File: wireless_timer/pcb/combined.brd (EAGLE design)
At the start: 36 x 76.5 mm, 51 parts, among them U1 ATTINY1616-SNR

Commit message: ready for dcdc insertion
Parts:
- removed C8: 10uF, rcl:C0805
- moved D1 12.4 mm to (8.52, 33.8), turned to 180 degrees
- moved R21 9.14 mm to (32.7, 25.8)
- moved C9 5.55 mm to (14.1, 35.6)
- moved JP3 4.20 mm to (33.9, 36.3)
- moved TP4 4.20 mm to (19.2, 51.3)
- moved JP5 4.20 mm to (33.8, 45.8)
- moved R1 4.20 mm to (22.0, 47.5)
- moved R16 4.20 mm to (30.4, 46.9)
- moved R18 4.20 mm to (31.2, 35.6)
- moved R2 4.20 mm to (19.7, 47.5)
- moved TP5 4.20 mm to (25.2, 51.3)
- moved C1 4.20 mm to (17.8, 47.6)
- moved R15 4.20 mm to (30.4, 49.1)
- moved R17 4.20 mm to (31.3, 43.5)
- moved R20 4.20 mm to (24.2, 47.6)
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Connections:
- net GND: no longer C8.2
- net VCC: no longer C8.1

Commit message: layout completed
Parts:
- added C17, C18, C19: 10uF, rcl:C0805
- added D2, D3: BAT, diode:SOD-123_MINI-SMA
- added JP6, JP7: (no value), pinhead-2:1X02-S
- added L1: 1uH, 5040_INDUCTOR:IND_74404043220A
- added R22, R23: 100K, rcl:R0805
- added R38: 511K, rcl:M0805
- added R39: 91K, rcl:M0805
- added R45: 50K, rcl:M0805
- added U2: TPS, TPS63000DRLR:SOTFL50P160X60-8N
- added U3, U4: PMOS, DMP3165L:SOT103P240X110-3N
- S1, S2, S3, S4, S5, S6: value SW_55MM -> SW
- TP1, TP5: value TPTP18R -> GND
- TP2: value TPTP18R -> VDD
- TP3: value TPTP18R -> VCC
- TP4: value TPTP18R -> VBAT
- U1: value ATTINY1616-SNR -> 1
- moved D1 27.7 mm to (7.12, 61.5), flipped to the bottom, turned to 270 degrees
- moved TP4 19.1 mm to (32.4, 65.2), turned to 180 degrees
- moved TP3 14.7 mm to (23.1, 57.6)
- moved TP2 14.2 mm to (15.3, 51.3), turned to 270 degrees
- moved R21 13.6 mm to (31.3, 39.4), flipped to the bottom
- moved TP5 6.75 mm to (18.5, 51.3)
- moved JP4 6.17 mm to (32.5, 61.1), flipped to the top
- moved JP2 5.23 mm to (3.60, 61.1), flipped to the bottom
- moved C9 0.88 mm to (14.0, 36.5), turned to 270 degrees
- moved R3 0.53 mm to (24.1, 31.7)
- moved R18 0.44 mm to (31.2, 35.2)
- moved R4 0.42 mm to (24.1, 29.4)
- moved C1 0.32 mm to (17.4, 47.5)
- moved C2 0.30 mm to (24.1, 27.1)
- moved R1 0.07 mm to (21.9, 47.6)
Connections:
- new net DC_SW: R22.1, U1.3, U3.1
- new net LX1: L1.2, U2.3
- new net LX2: L1.1, U2.2
- new net N$27: R38.1, R39.2, U2.8
- new net N$36: R45.2, U2.5
- new net VBAT_O: D1.A, D3.A, JP6.2, JP7.2, R1.2, R22.2, U3.2
- new net VCC_SW: R23.2, U1.5, U4.1
- new net VIN: C17.1, D3.C, U2.4, U3.3
- net GND: now also C17.2, C18.2, C19.2, R39.1, R45.1, U2.7
- net S6: no longer TP3.TP
- net SHDN: now also U2.6
- net VBAT: now also JP6.1, JP7.1; no longer D1.A, R1.2
- net VCC: now also C18.1, C19.1, D2.A, R23.1, R38.2, TP3.TP, U2.1, U4.2
- net VDD: now also D2.C, U4.3
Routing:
- net GND: track 0.00 -> 307.2 mm, vias 0 -> 5
- net VCC: track 0.00 -> 191.0 mm, vias 0 -> 9
- net VDD: track 0.00 -> 100.5 mm, vias 0 -> 1
- net SCL: track 0.00 -> 88.3 mm, vias 0 -> 2
- net S3: track 0.00 -> 60.7 mm, vias 0 -> 3
- net VBAT_O: track 0.00 -> 45.7 mm, vias 0 -> 1
- net VBAT: track 0.00 -> 43.7 mm
- net S6: track 0.00 -> 37.4 mm, vias 0 -> 3
- net S4: track 0.00 -> 34.6 mm, vias 0 -> 3
- net S2: track 0.00 -> 29.7 mm, vias 0 -> 3
- net SDA: track 0.00 -> 28.0 mm, vias 0 -> 3
- net DC_SW: track 0.00 -> 27.8 mm, vias 0 -> 2
- net SHDN: track 0.00 -> 25.4 mm, vias 0 -> 3
- net SET: track 0.00 -> 24.4 mm, vias 0 -> 4
- net S5: track 0.00 -> 23.6 mm, vias 0 -> 3
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- added copper zone on layer 1, net GND
- added copper zone on layer 16, net GND
- added copper zone on layer 16, net LX1
- added copper zone on layer 16, net LX2
- added copper zone on layer 16, net VCC
- added copper zone on layer 16, net VIN
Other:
- board text added: "+"
- board text added: "-"
- board text added: "1"
- board text added: "K"
- board text added: "SCL"
- board text added: "SDA"
- board text added: "VCC"
- board text added: "_/ _"

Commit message: panel made, outline pending
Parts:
- added A2: 1X05, pinhead_smd:1X05X254
- added C12: 10uF, rcl:CT3528
- added C13, C14, C15, C16, C20, C21, C8: 100nF, rcl:C0805
- added C22, C23, C24, C25, C26: 10uF, rcl:C0805
- added D4, D5, D6: BAT, diode:SOD-123_MINI-SMA
- added JP10, JP9: (no value), pinhead-2:1X04-S
- added JP11, JP12, JP13, JP14: (no value), pinhead-2:1X02-S
- added JP8: (no value), pinhead-2:1X03-S
- added L2: 1uH, 5040_INDUCTOR:IND_74404043220A
- added R24, R25, R36, R46: 30K, rcl:R0805
- added R26, R27, R28, R29, R30, R31, R32, R33, R34, R35, R37, R40: 10K, rcl:R0805
- added R41, R42, R51, R52: 100K, rcl:R0805
- added R43, R44: 1K, rcl:R0805
- added R47: 200E, rcl:R0805
- added R48: 511K, rcl:M0805
- added R49: 91K, rcl:M0805
- added R50: 50K, rcl:M0805
- added S10, S11, S12, S7, S8, S9: SW, switch_5p5mm:SW_55MM
- added TP10: VCC, testpad:TP18R
- added TP6: VBAT, testpad:TP18R
- added TP7, TP8: GND, testpad:TP18R
- added TP9: VDD, testpad:TP18R
- added U5: 1, ATTINY1616-SNR:SOIC127P1032X265-20N
- added U6: TPS, TPS63000DRLR:SOTFL50P160X60-8N
- added U7, U8: PMOS, DMP3165L:SOT103P240X110-3N
- moved C9 1.51 mm to (14.0, 38.0)
- moved D2 1.51 mm to (15.0, 44.3)
- moved JP1 1.51 mm to (18.0, 67.0)
- moved JP5 1.51 mm to (33.8, 47.3)
- moved R2 1.51 mm to (19.6, 49.1)
- moved R22 1.51 mm to (10.6, 57.1)
- moved R23 1.51 mm to (26.9, 59.1)
- moved R38 1.51 mm to (6.54, 48.4)
- moved R45 1.51 mm to (7.82, 47.5)
- moved TP1 1.51 mm to (13.9, 69.6)
- moved TP4 1.51 mm to (32.4, 66.7)
- moved A1 1.51 mm to (18.0, 26.5)
- moved C10 1.51 mm to (12.8, 30.1)
- moved R4 1.51 mm to (24.1, 30.9)
- moved R6 1.51 mm to (4.32, 24.9)
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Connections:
- new net DC_SW1: R51.1, U5.3, U7.1
- new net GND1: A2.2, C12.-, C13.2, C14.2, C15.2, C16.2, C20.2, C21.2, C22.2, C23.2, C24.2, C25.2, C26.2, C8.2, JP10.4, JP11.2, JP12.2, JP8.2, JP9.4, R36.1, R42.2, R46.1, R49.1, R50.1, S10.3, S10.4, S11.3, S11.4, S12.3, S12.4, S7.3, S7.4, S8.3, S8.4, S9.3, S9.4, TP7.TP, TP8.TP, U5.20, U6.7
- new net LX3: L2.2, U6.3
- new net LX4: L2.1, U6.2
- new net N$11: R32.1, R33.2, S10.1, S10.2
- new net N$13: R34.1, R35.2, S11.1, S11.2
- new net N$14: R37.1, R40.2, S12.1, S12.2
- new net N$15: JP8.3, U5.16
- new net N$16: JP8.1, R47.2
- new net N$17: R48.1, R49.2, U6.8
- new net N$18: R50.2, U6.5
- new net N$4: R26.1, R27.2, S7.1, S7.2
- new net N$6: R28.1, R29.2, S8.1, S8.2
- new net N$7: R30.1, R31.2, S9.1, S9.2
- new net RXD02: R44.2, U5.8
- new net RXD03: A2.4, U5.18
- new net RXD04: JP9.3, R44.1
- new net S10: C15.1, R33.1, U5.19
- new net S11: C16.1, R35.1, U5.15
- new net S12: C20.1, R40.1, U5.4
- new net S7: C8.1, R27.1, U5.12
- new net S8: C13.1, R29.1, U5.13
- new net S9: C14.1, R31.1, U5.14
- new net SCL1: JP10.2, R25.2, U5.11
- new net SDA1: JP10.1, R24.2, U5.10
- new net SET1: A2.5, R36.2, U5.7
- new net SHDN1: R46.2, U5.6, U6.6
- new net TXD02: R43.2, U5.9
- new net TXD03: A2.3, U5.17
- new net TXD04: JP9.2, R43.1
- new net VADC1: C21.1, R41.1, R42.1, U5.2
- new net VBAT1: JP11.1, JP12.1, JP13.1, JP14.1, TP6.TP
- new net VBAT_O1: D4.A, D6.A, JP13.2, JP14.2, R41.2, R51.2, U7.2
- new net VCC1: A2.1, C12.+, C22.1, C23.1, C25.1, C26.1, D5.A, JP10.3, R24.1, R25.1, R26.2, R28.2, R30.2, R32.2, R34.2, R48.2, R52.1, TP10.TP, U6.1, U8.2
- new net VCC_SW1: R52.2, U5.5, U8.1
- new net VDD1: D4.C, D5.C, JP9.1, R37.2, R47.1, TP9.TP, U5.1, U8.3
- new net VIN1: C24.1, D6.C, U6.4, U7.3
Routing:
- net GND1: track 0.00 -> 307.2 mm, vias 0 -> 5
- net VCC1: track 0.00 -> 191.0 mm, vias 0 -> 9
- net VDD1: track 0.00 -> 100.5 mm, vias 0 -> 1
- net SCL1: track 0.00 -> 88.3 mm, vias 0 -> 2
- net S9: track 0.00 -> 60.7 mm, vias 0 -> 3
- net VBAT_O1: track 0.00 -> 45.7 mm, vias 0 -> 1
- net VBAT1: track 0.00 -> 43.7 mm
- net S12: track 0.00 -> 37.4 mm, vias 0 -> 3
- net S10: track 0.00 -> 34.6 mm, vias 0 -> 3
- net S8: track 0.00 -> 29.7 mm, vias 0 -> 3
- net SDA1: track 0.00 -> 28.0 mm, vias 0 -> 3
- net DC_SW1: track 0.00 -> 27.8 mm, vias 0 -> 2
- net SHDN1: track 0.00 -> 25.4 mm, vias 0 -> 3
- net SET1: track 0.00 -> 24.4 mm, vias 0 -> 4
- net S11: track 0.00 -> 23.6 mm, vias 0 -> 3
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- added copper zone on layer 1, net GND1
- added copper zone on layer 16, net GND1
- added copper zone on layer 16, net LX3
- added copper zone on layer 16, net LX4
- added copper zone on layer 16, net VCC1
- added copper zone on layer 16, net VIN1
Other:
- board size 36 x 76.5 mm -> 74 x 76.5 mm
- board text added: "A1"
- board text added: "C1"
- board text added: "C10"
- board text added: "C11"
- board text added: "C17"
- board text added: "C18"
- board text added: "C19"
- board text added: "C2"
- board text added: "C3"
- board text added: "C4"
- board text added: "C5"
- board text added: "C6"
- board text added: "C7"
- board text added: "C9"
- board text added: "D1"
- board text added: "D2"
- board text added: "D3"
- board text added: "JP1"
- board text added: "JP2"
- board text added: "JP3"
- board text added: "JP4"
- board text added: "JP5"
- board text added: "JP6"
- board text added: "JP7"
- board text added: "L1"
- board text added: "R1"
- board text added: "R10"
- board text added: "R11"
- board text added: "R12"
- board text added: "R13"
- board text added: "R14"
- board text added: "R15"
- board text added: "R16"
- board text added: "R17"
- board text added: "R18"
- board text added: "R19"
- board text added: "R2"
- board text added: "R20"
- board text added: "R21"
- board text added: "R22"
- board text added: "R23"
- board text added: "R3"
- board text added: "R38"
- board text added: "R39"
- board text added: "R4"
- board text added: "R45"
- board text added: "R5"
- board text added: "R6"
- board text added: "R7"
- board text added: "R8"
- board text added: "R9"
- board text added: "S1"
- board text added: "S2"
- board text added: "S3"
- board text added: "S4"
- board text added: "S5"
- board text added: "S6"
- board text added: "TP1"
- board text added: "TP2"
- board text added: "TP3"
- board text added: "TP4"
- board text added: "TP5"
- board text added: "U1"
- board text added: "U2"
- board text added: "U3"
- board text added: "U4"

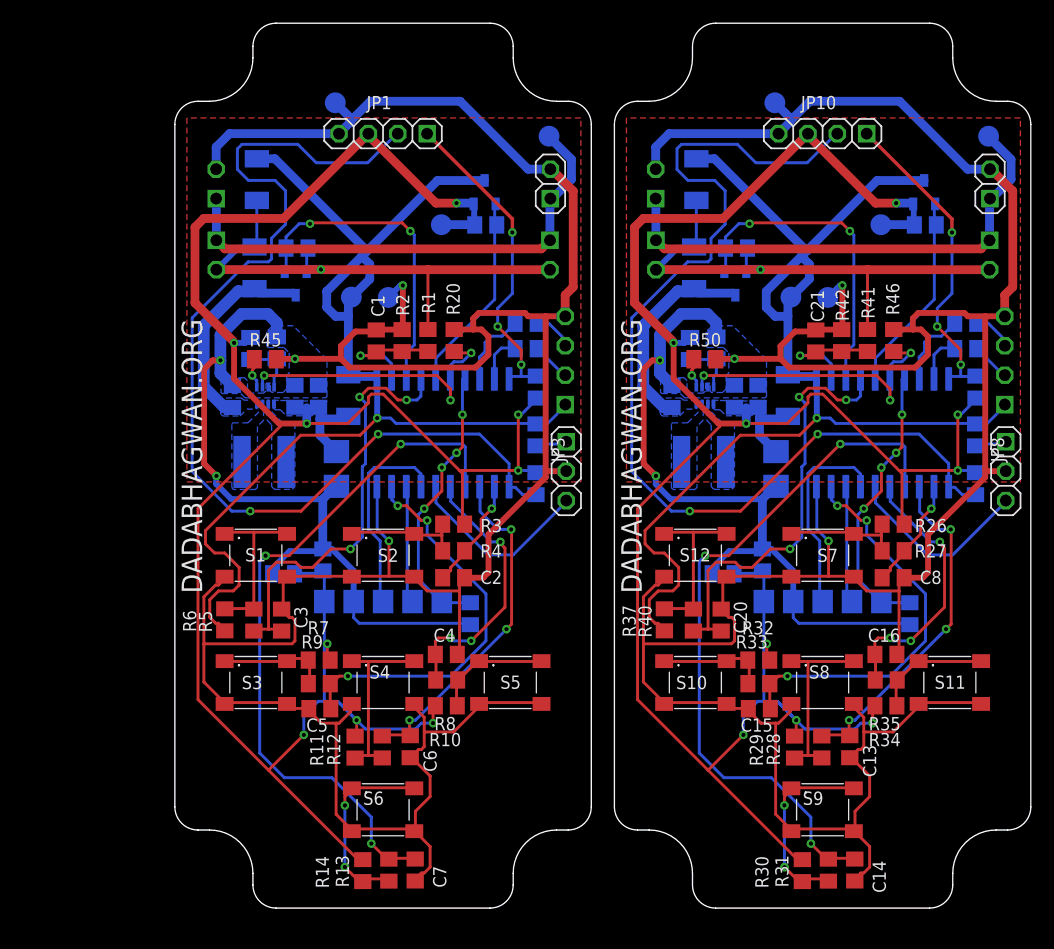
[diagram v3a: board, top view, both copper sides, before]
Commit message: panel completed, outline added
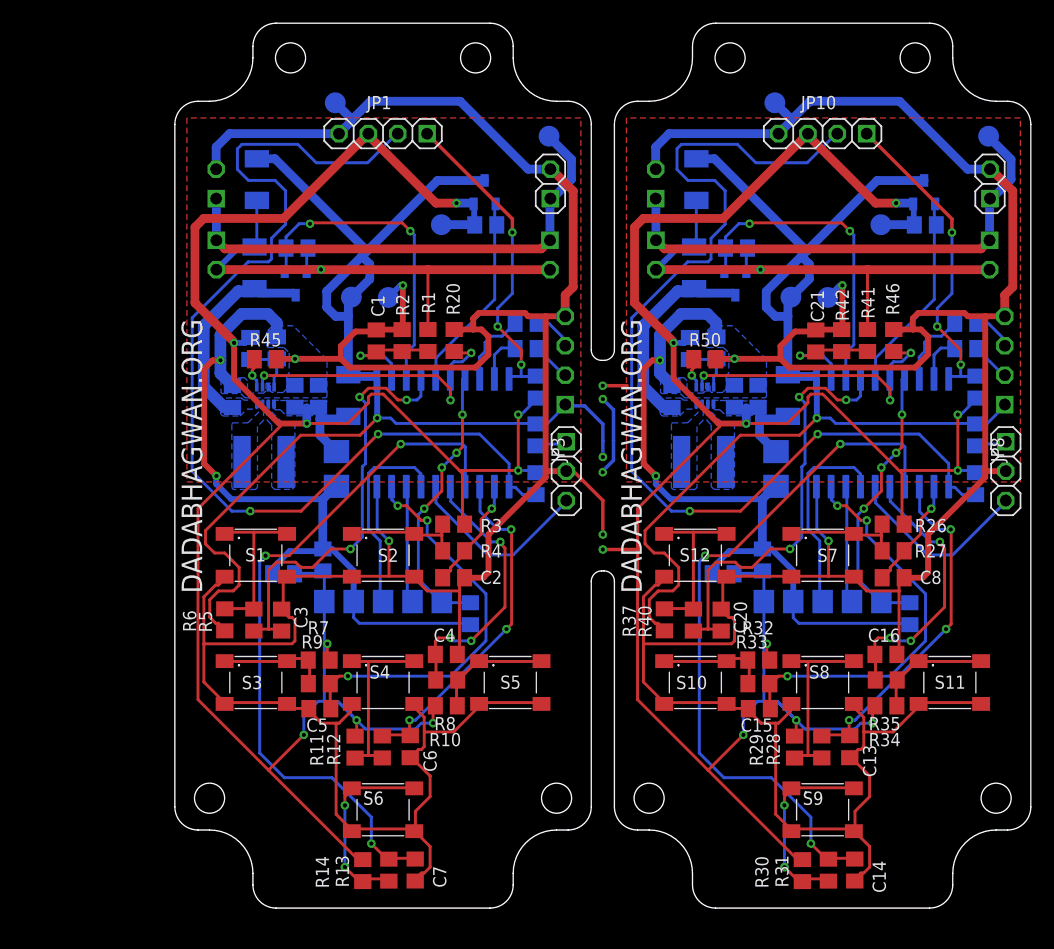
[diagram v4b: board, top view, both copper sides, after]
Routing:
- net GND: track 307.2 -> 314.4 mm, vias 5 -> 6
- net SDF: track 0.00 -> 7.09 mm, vias 0 -> 2
- net VDD: track 100.5 -> 107.2 mm, vias 1 -> 2
- net VCC1: track 191.0 -> 194.1 mm, vias 9 -> 10
- net GND1: track 307.2 -> 309.3 mm, vias 5 -> 6
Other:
- outline, holes or cut-outs redrawn
